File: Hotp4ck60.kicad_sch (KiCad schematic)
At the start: 46 parts, among them J1 HRO_TYPE-C-31-M-12, SW44 RST, U1 nRF52840, U2 SRV05-4, Y1 32 MHz, Y2 32.768 Khz

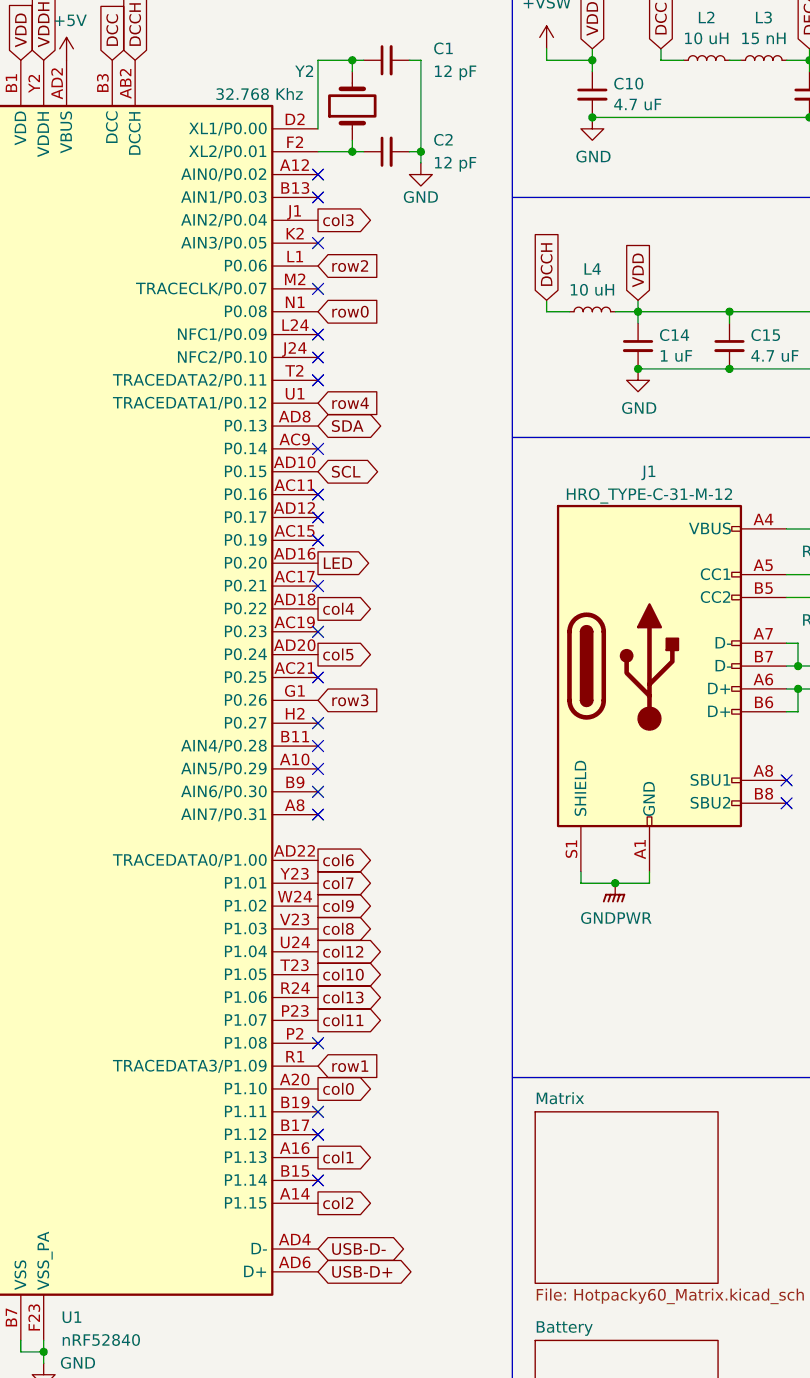
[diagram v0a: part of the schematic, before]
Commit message: replace parts and change pin assignment.
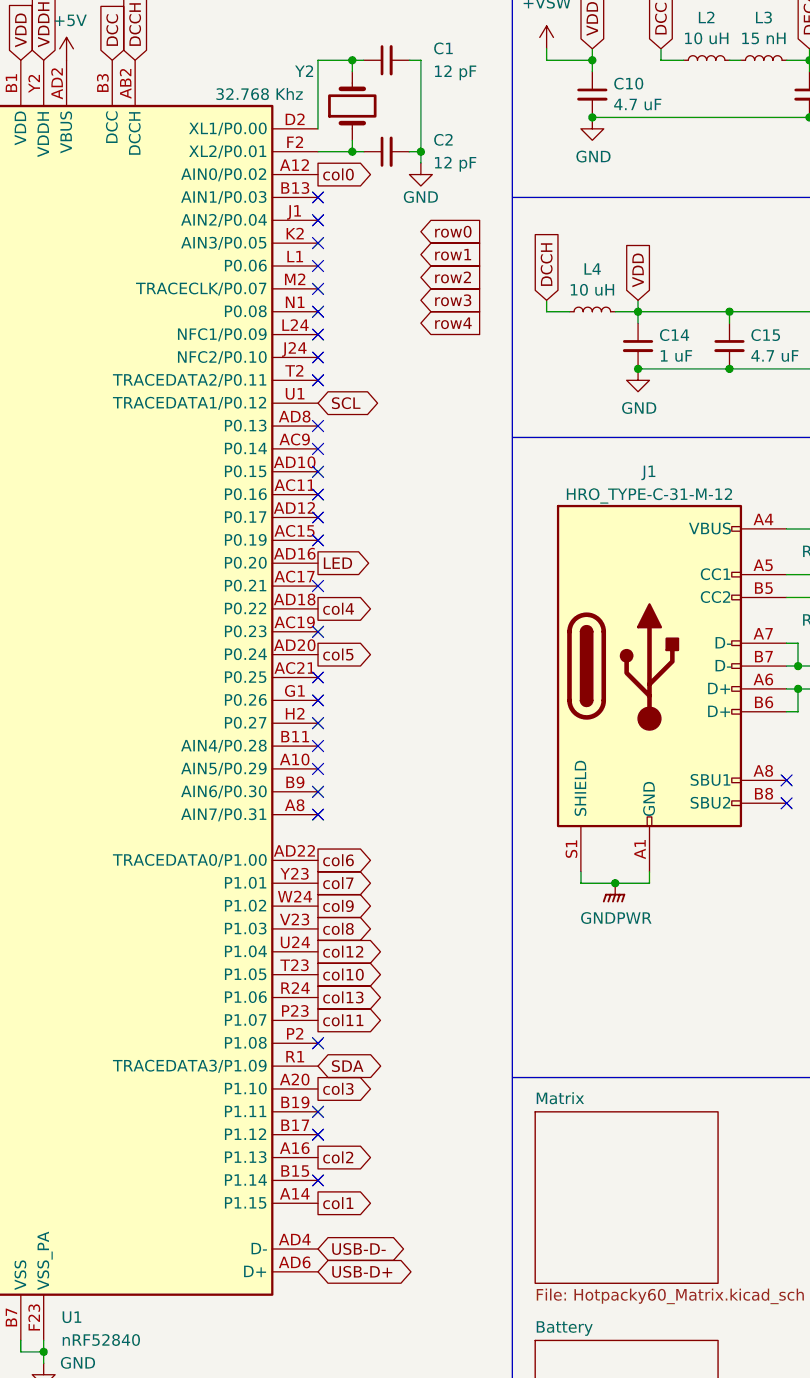
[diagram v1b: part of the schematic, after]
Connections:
- net SCL: now also U1.U1 (TRACEDATA1/P0.12); no longer U1.AD10 (P0.15)
- net SDA: now also U1.R1 (TRACEDATA3/P1.09); no longer U1.AD8 (P0.13)
- net col0: now also U1.A12 (AIN0/P0.02); no longer U1.A20 (P1.10)
- net col1: now also U1.A14 (P1.15); no longer U1.A16 (P1.13)
- net col2: now also U1.A16 (P1.13); no longer U1.A14 (P1.15)
- net col3: now also U1.A20 (P1.10); no longer U1.J1 (AIN2/P0.04)
- net row0: no longer U1.N1 (P0.08)
- net row1: no longer U1.R1 (TRACEDATA3/P1.09)
- net row2: no longer U1.L1 (P0.06)
- net row3: no longer U1.G1 (P0.26)
- net row4: no longer U1.U1 (TRACEDATA1/P0.12)
- no-connect marks 28 -> 33
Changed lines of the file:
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@@
   (no_connect (at 102.87 44.45))
   (no_connect (at 102.87 59.69))
+  (no_connect (at 102.87 52.07))
   (no_connect (at 52.07 24.13))
   (no_connect (at 154.94 104.14))
@@
   (no_connect (at 102.87 97.79))
   (no_connect (at 212.09 120.65))
+  (no_connect (at 102.87 41.91))
   (no_connect (at 102.87 77.47))
+  (no_connect (at 102.87 95.25))
   (no_connect (at 102.87 87.63))
   (no_connect (at 102.87 67.31))
@@
   (no_connect (at 102.87 74.93))
   (no_connect (at 102.87 82.55))
-  (no_connect (at 102.87 36.83))
+  (no_connect (at 102.87 46.99))
   (no_connect (at 102.87 133.35))
   (no_connect (at 102.87 54.61))
@@
   (no_connect (at 102.87 49.53))
   (no_connect (at 102.87 143.51))
+  (no_connect (at 102.87 69.85))
   (no_connect (at 102.87 100.33))
+  (no_connect (at 102.87 64.77))
   (no_connect (at 102.87 140.97))
   (no_connect (at 102.87 92.71))
@@
     (stroke (width 0) (type default))
   )
+  (global_label "SCL" (shape bidirectional) (at 102.87 62.23 0) (fields_autoplaced)
+    (effects (font (size 1.27 1.27)) (justify left))
+    (property "Intersheetrefs" "${INTERSHEET_REFS}" (at 108.7907 62.1506 0)
+      (effects (font (size 1.27 1.27)) (justify left) hide)
+    )
+  )
   (global_label "DEC1" (shape input) (at 200.66 22.86 90) (fields_autoplaced)
     (effects (font (size 1.27 1.27)) (justify left))
@@
     )
   )
-  (global_label "row2" (shape input) (at 102.87 46.99 0) (fields_autoplaced)
-    (effects (font (size 1.27 1.27)) (justify left))
-    (property "Intersheetrefs" "${INTERSHEET_REFS}" (at 110.251 46.99 0)
-      (effects (font (size 1.27 1.27)) (justify left) hide)
-    )
-  )
   (global_label "DEC4_6" (shape input) (at 157.48 22.86 90) (fields_autoplaced)
     (effects (font (size 1.27 1.27)) (justify left))
@@
     )
   )
-  (global_label "col3" (shape output) (at 102.87 41.91 0) (fields_autoplaced)
-    (effects (font (size 1.27 1.27)) (justify left))
-    (property "Intersheetrefs" "${INTERSHEET_REFS}" (at 109.8881 41.91 0)
+  (global_label "col3" (shape output) (at 102.87 138.43 0) (fields_autoplaced)
+    (effects (font (size 1.27 1.27)) (justify left))
+    (property "Intersheetrefs" "${INTERSHEET_REFS}" (at 109.8881 138.43 0)
       (effects (font (size 1.27 1.27)) (justify left) hide)
     )
@@
     )
   )
+  (global_label "col1" (shape output) (at 102.87 151.13 0) (fields_autoplaced)
+    (effects (font (size 1.27 1.27)) (justify left))
+    (property "Intersheetrefs" "${INTERSHEET_REFS}" (at 109.8881 151.13 0)
+      (effects (font (size 1.27 1.27)) (justify left) hide)
+    )
+  )
   (global_label "DCCH" (shape input) (at 128.27 50.8 90) (fields_autoplaced)
     (effects (font (size 1.27 1.27)) (justify left))
@@
     )
   )
+  (global_label "row2" (shape input) (at 114.3 48.26 0) (fields_autoplaced)
+    (effects (font (size 1.27 1.27)) (justify left))
+    (property "Intersheetrefs" "${INTERSHEET_REFS}" (at 121.681 48.26 0)
+      (effects (font (size 1.27 1.27)) (justify left) hide)
+    )
+  )
   (global_label "VBUS" (shape input) (at 170.18 105.41 180) (fields_autoplaced)
     (effects (font (size 1.27 1.27)) (justify right))
@@
     )
   )
+  (global_label "SDA" (shape bidirectional) (at 102.87 135.89 0) (fields_autoplaced)
+    (effects (font (size 1.27 1.27)) (justify left))
+    (property "Intersheetrefs" "${INTERSHEET_REFS}" (at 108.8512 135.8106 0)
+      (effects (font (size 1.27 1.27)) (justify left) hide)
+    )
+  )
+  (global_label "row0" (shape input) (at 114.3 43.18 0) (fields_autoplaced)
+    (effects (font (size 1.27 1.27)) (justify left))
+    (property "Intersheetrefs" "${INTERSHEET_REFS}" (at 121.681 43.18 0)
+      (effects (font (size 1.27 1.27)) (justify left) hide)
+    )
+  )
   (global_label "RST" (shape output) (at 273.05 24.13 0) (fields_autoplaced)
     (effects (font (size 1.27 1.27)) (justify left))
@@
     )
   )
+  (global_label "row1" (shape input) (at 114.3 45.72 0) (fields_autoplaced)
+    (effects (font (size 1.27 1.27)) (justify left))
+    (property "Intersheetrefs" "${INTERSHEET_REFS}" (at 121.681 45.72 0)
+      (effects (font (size 1.27 1.27)) (justify left) hide)
+    )
+  )
   (global_label "VDD" (shape input) (at 138.43 50.8 90) (fields_autoplaced)
     (effects (font (size 1.27 1.27)) (justify left))
@@
     )
   )
-  (global_label "SCL" (shape bidirectional) (at 102.87 69.85 0) (fields_autoplaced)
-    (effects (font (size 1.27 1.27)) (justify left))
-    (property "Intersheetrefs" "${INTERSHEET_REFS}" (at 108.7907 69.7706 0)
-      (effects (font (size 1.27 1.27)) (justify left) hide)
-    )
-  )
-  (global_label "row4" (shape input) (at 102.87 62.23 0) (fields_autoplaced)
-    (effects (font (size 1.27 1.27)) (justify left))
-    (property "Intersheetrefs" "${INTERSHEET_REFS}" (at 110.251 62.23 0)
-      (effects (font (size 1.27 1.27)) (justify left) hide)
-    )
-  )
-  (global_label "row0" (shape input) (at 102.87 52.07 0) (fields_autoplaced)
-    (effects (font (size 1.27 1.27)) (justify left))
-    (property "Intersheetrefs" "${INTERSHEET_REFS}" (at 110.251 52.07 0)
+  (global_label "row4" (shape input) (at 114.3 53.34 0) (fields_autoplaced)
+    (effects (font (size 1.27 1.27)) (justify left))
+    (property "Intersheetrefs" "${INTERSHEET_REFS}" (at 121.681 53.34 0)
+      (effects (font (size 1.27 1.27)) (justify left) hide)
+    )
+  )
+  (global_label "col0" (shape output) (at 102.87 36.83 0) (fields_autoplaced)
+    (effects (font (size 1.27 1.27)) (justify left))
+    (property "Intersheetrefs" "${INTERSHEET_REFS}" (at 109.8881 36.83 0)
       (effects (font (size 1.27 1.27)) (justify left) hide)
     )
@@
     )
   )
-  (global_label "col0" (shape output) (at 102.87 138.43 0) (fields_autoplaced)
-    (effects (font (size 1.27 1.27)) (justify left))
-    (property "Intersheetrefs" "${INTERSHEET_REFS}" (at 109.8881 138.43 0)
-      (effects (font (size 1.27 1.27)) (justify left) hide)
-    )
-  )
   (global_label "DEC5" (shape input) (at 59.69 24.13 90) (fields_autoplaced)
     (effects (font (size 1.27 1.27)) (justify left))
@@
     )
   )
-  (global_label "SDA" (shape bidirectional) (at 102.87 64.77 0) (fields_autoplaced)
-    (effects (font (size 1.27 1.27)) (justify left))
-    (property "Intersheetrefs" "${INTERSHEET_REFS}" (at 108.8512 64.6906 0)
-      (effects (font (size 1.27 1.27)) (justify left) hide)
-    )
-  )
-  (global_label "row1" (shape input) (at 102.87 135.89 0) (fields_autoplaced)
-    (effects (font (size 1.27 1.27)) (justify left))
-    (property "Intersheetrefs" "${INTERSHEET_REFS}" (at 110.251 135.89 0)
-      (effects (font (size 1.27 1.27)) (justify left) hide)
-    )
-  )
   (global_label "SWDCLK" (shape output) (at 236.22 43.18 180) (fields_autoplaced)
     (effects (font (size 1.27 1.27)) (justify right))
@@
     )
   )
-  (global_label "col1" (shape output) (at 102.87 146.05 0) (fields_autoplaced)
+  (global_label "col2" (shape output) (at 102.87 146.05 0) (fields_autoplaced)
     (effects (font (size 1.27 1.27)) (justify left))
     (property "Intersheetrefs" "${INTERSHEET_REFS}" (at 109.8881 146.05 0)
@@
     )
   )
-  (global_label "col2" (shape output) (at 102.87 151.13 0) (fields_autoplaced)
-    (effects (font (size 1.27 1.27)) (justify left))
-    (property "Intersheetrefs" "${INTERSHEET_REFS}" (at 109.8881 151.13 0)
-      (effects (font (size 1.27 1.27)) (justify left) hide)
-    )
-  )
   (global_label "col8" (shape output) (at 102.87 120.65 0) (fields_autoplaced)
     (effects (font (size 1.27 1.27)) (justify left))
@@
     )
   )
-  (global_label "row3" (shape input) (at 102.87 95.25 0) (fields_autoplaced)
-    (effects (font (size 1.27 1.27)) (justify left))
-    (property "Intersheetrefs" "${INTERSHEET_REFS}" (at 110.251 95.25 0)
-      (effects (font (size 1.27 1.27)) (justify left) hide)
-    )
+  (global_label "row3" (shape input) (at 114.3 50.8 0) (fields_autoplaced)
+    (effects (font (size 1.27 1.27)) (justify left))
+    (property "Intersheetrefs" "${INTERSHEET_REFS}" (at 121.681 50.8 0)
+      (effects (font (size 1.27 1.27)) (justify left) hide)
+    )

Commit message: Routing finished
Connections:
- net LED: now also U1.A10 (AIN5/P0.29); no longer U1.AD16 (P0.20)
- net col10: now also U1.P23 (P1.07); no longer U1.T23 (P1.05)
- net col11: now also U1.W24 (P1.02); no longer U1.P23 (P1.07)
- net col4: now also U1.AD16 (P0.20); no longer U1.AD18 (P0.22)
- net col5: now also U1.Y23 (P1.01); no longer U1.AD20 (P0.24)
- net col6: now also U1.AD20 (P0.24); no longer U1.AD22 (TRACEDATA0/P1.00)
- net col7: now also U1.AD22 (TRACEDATA0/P1.00); no longer U1.Y23 (P1.01)
- net col9: now also U1.T23 (P1.05); no longer U1.W24 (P1.02)
- net row0: now also U1.AD8 (P0.13)
- net row1: now also U1.AD10 (P0.15)
- net row2: now also U1.AD12 (P0.17)
- net row3: now also U1.AD18 (P0.22)
- net row4: now also U1.N1 (P0.08)
- no-connect marks 33 -> 28

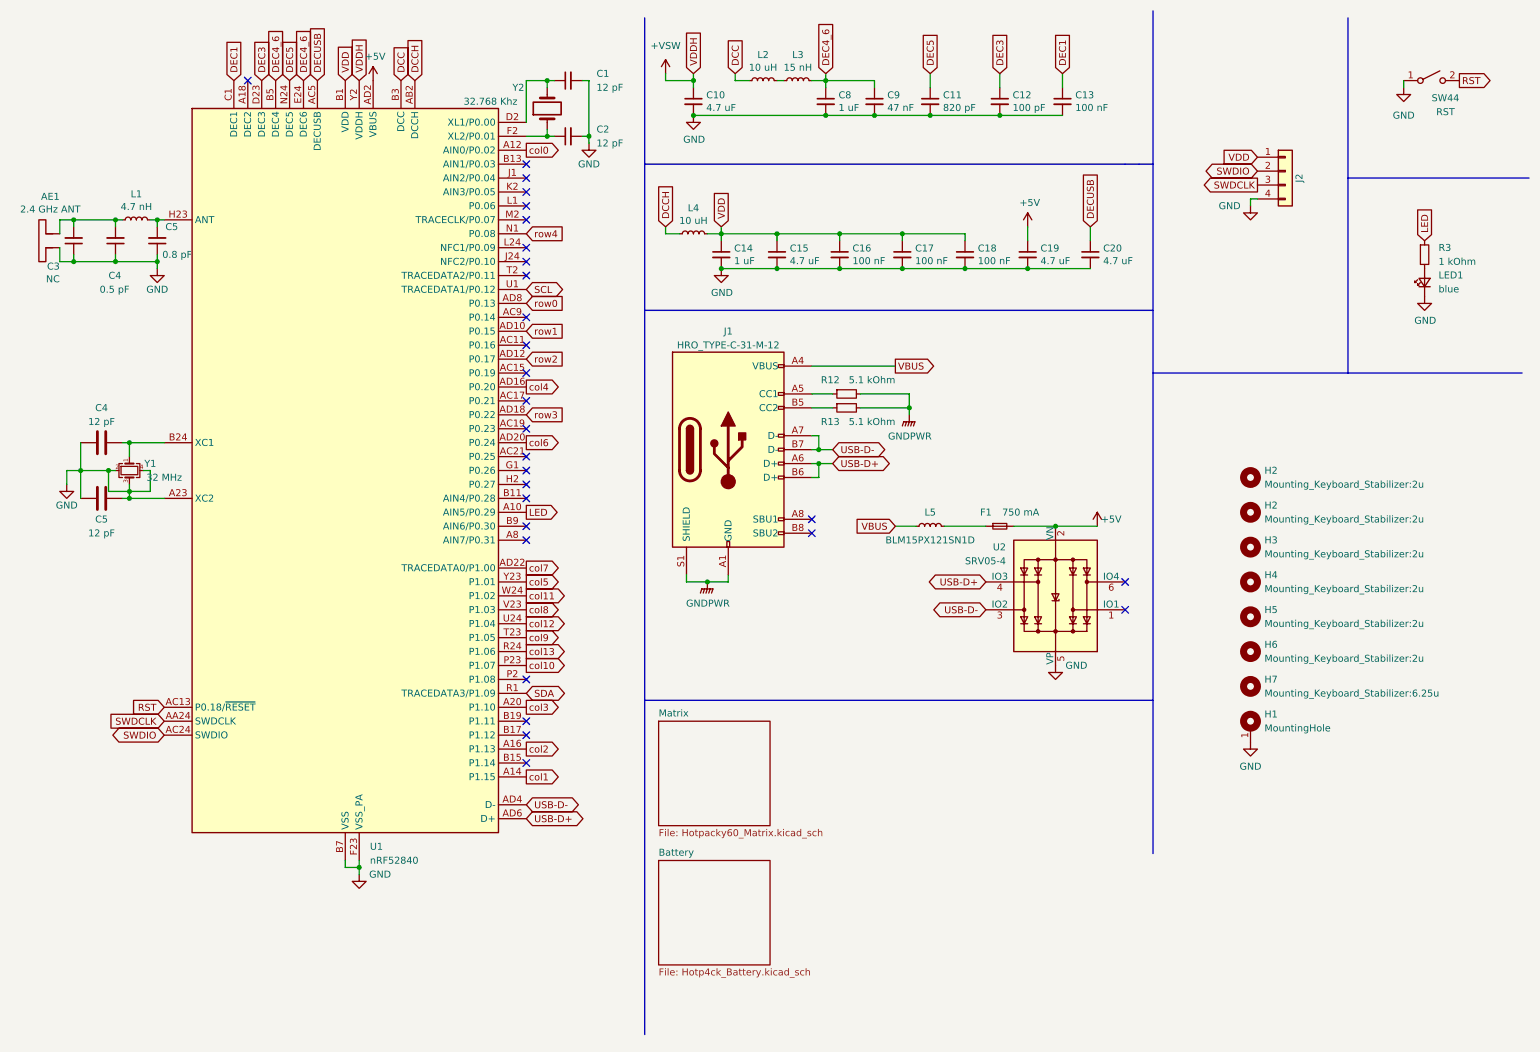
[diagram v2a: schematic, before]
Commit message: Enter LCSC parts numbers
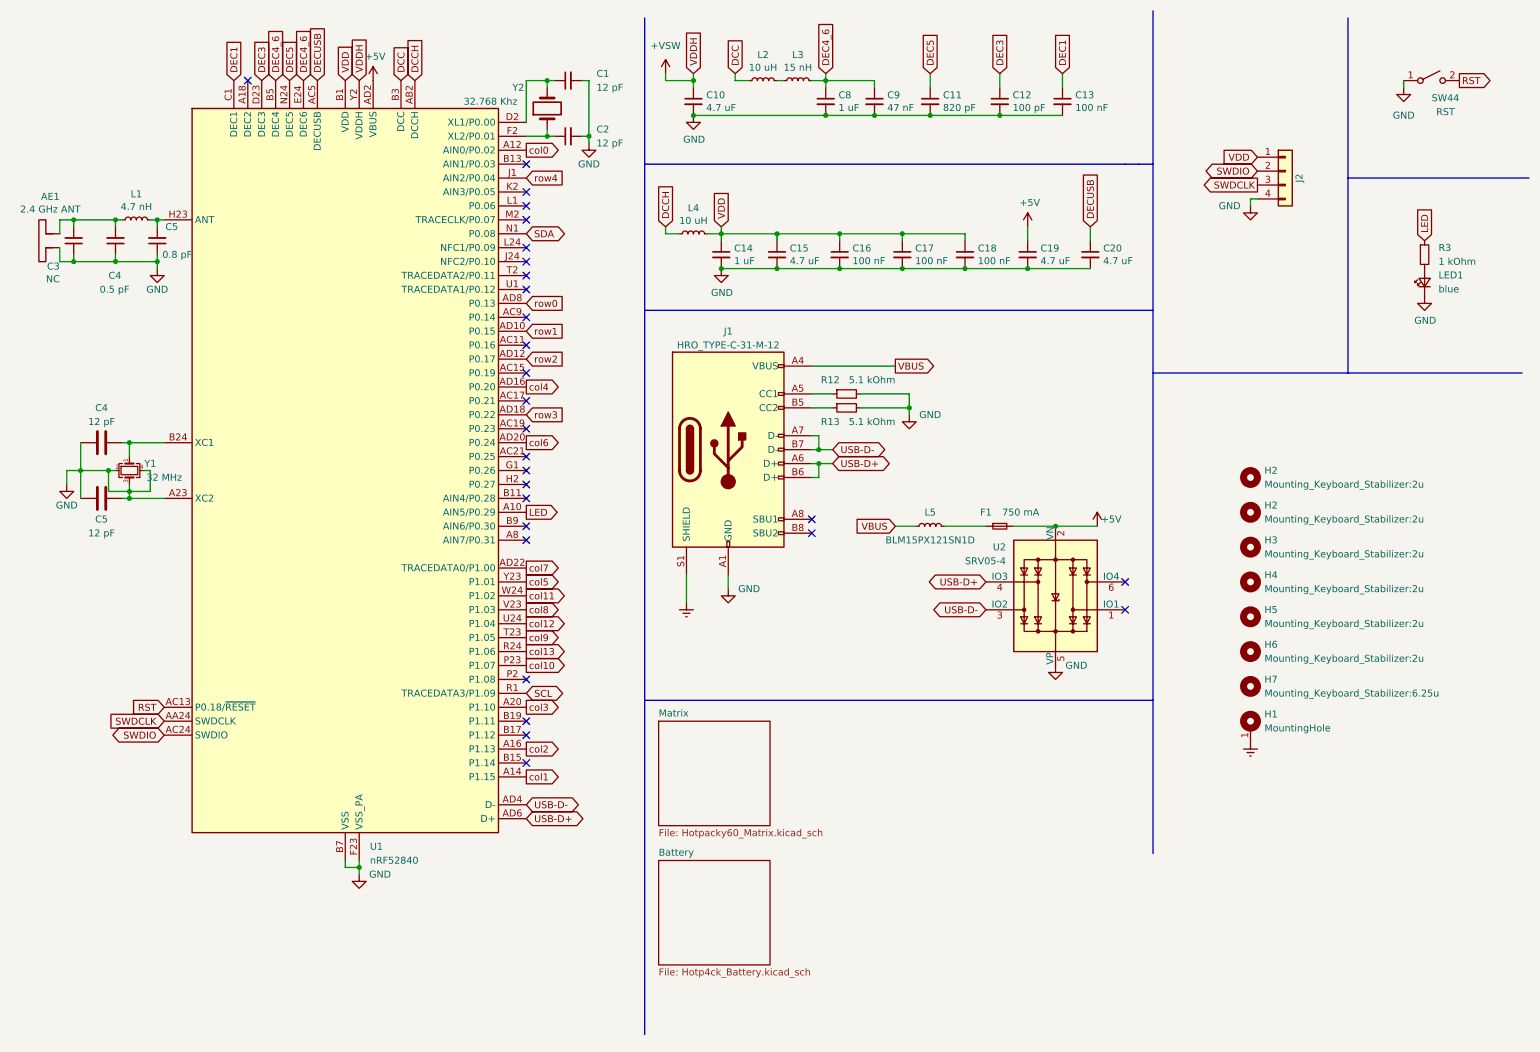
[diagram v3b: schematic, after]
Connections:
- net GND: now also J1.A1 (GND), J1.A12 (GND), J1.B1 (GND), J1.B12 (GND), R12.2, R13.2; no longer H1.1
- net SCL: now also U1.R1 (TRACEDATA3/P1.09); no longer U1.U1 (TRACEDATA1/P0.12)
- net SDA: now also U1.N1 (P0.08); no longer U1.R1 (TRACEDATA3/P1.09)
- net row4: now also U1.J1 (AIN2/P0.04); no longer U1.N1 (P0.08)
- removed net GNDPWR: J1.A1 (GND), J1.A12 (GND), J1.B1 (GND), J1.B12 (GND), J1.S1 (SHIELD), R12.2, R13.2
- new net Earth: H1.1, J1.S1 (SHIELD)

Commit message: Fixed position & etc..
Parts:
- added C14: 100nF, Capacitor_SMD:C_0402_1005Metric, symbol Device:C_Small
- added D64: D_TVS, Diode_SMD:D_SOD-123F, symbol Device:D_TVS
- added L5: BLM15PX121SN1D, Inductor_SMD:L_0402_1005Metric, symbol Device:L_Small
- added R13: 1 MOhm, Resistor_SMD:R_0402_1005Metric, symbol Device:R_Small
- LED1: footprint LED_SMD:LED_0402_1005Metric -> LED_SMD:LED_0603_1608Metric
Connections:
- net Earth: now also C14.1, R13.1
- net GND: now also D64.2 (A2), L5.1; no longer J1.A1 (GND), J1.A12 (GND), J1.B1 (GND), J1.B12 (GND), R12.2, R13.2
- net USB-D+: now also U2.6 (IO4); no longer U2.4 (IO3)
- net USB-D-: now also U2.1 (IO1); no longer U2.3 (IO2)
- new net GNDPWR: C14.2, D64.1 (A1), J1.A1 (GND), J1.A12 (GND), J1.B1 (GND), J1.B12 (GND), L5.2, R12.2, R13.2, R13.2
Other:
- moved on the sheet: F1, J1, L5, R12, R13, U2
